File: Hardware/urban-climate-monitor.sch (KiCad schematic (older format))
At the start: 44 parts, among them J1 Conn_ARM_JTAG_SWD_10, U1 AAT1217, U2 TPS27081A, U4 TSD305, U5 TSV911RILT, U6 RFM95W, U7 STM32L412KB

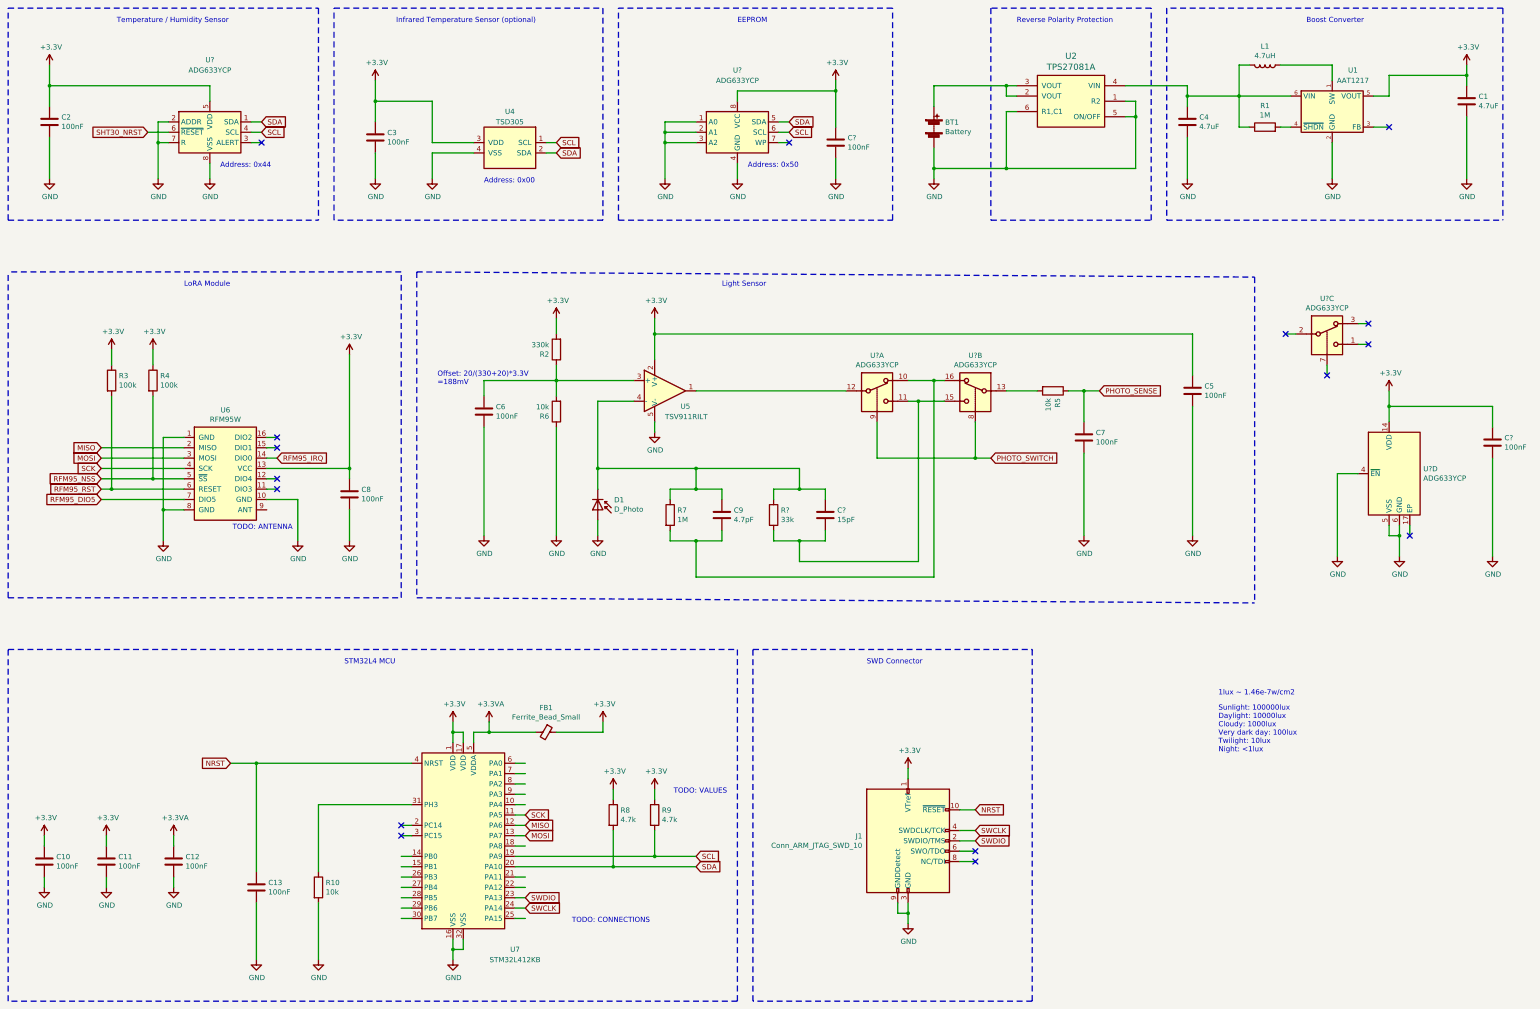
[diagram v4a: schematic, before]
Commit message: Create first revision of PCB, add CubeMX project for PCB sensor node
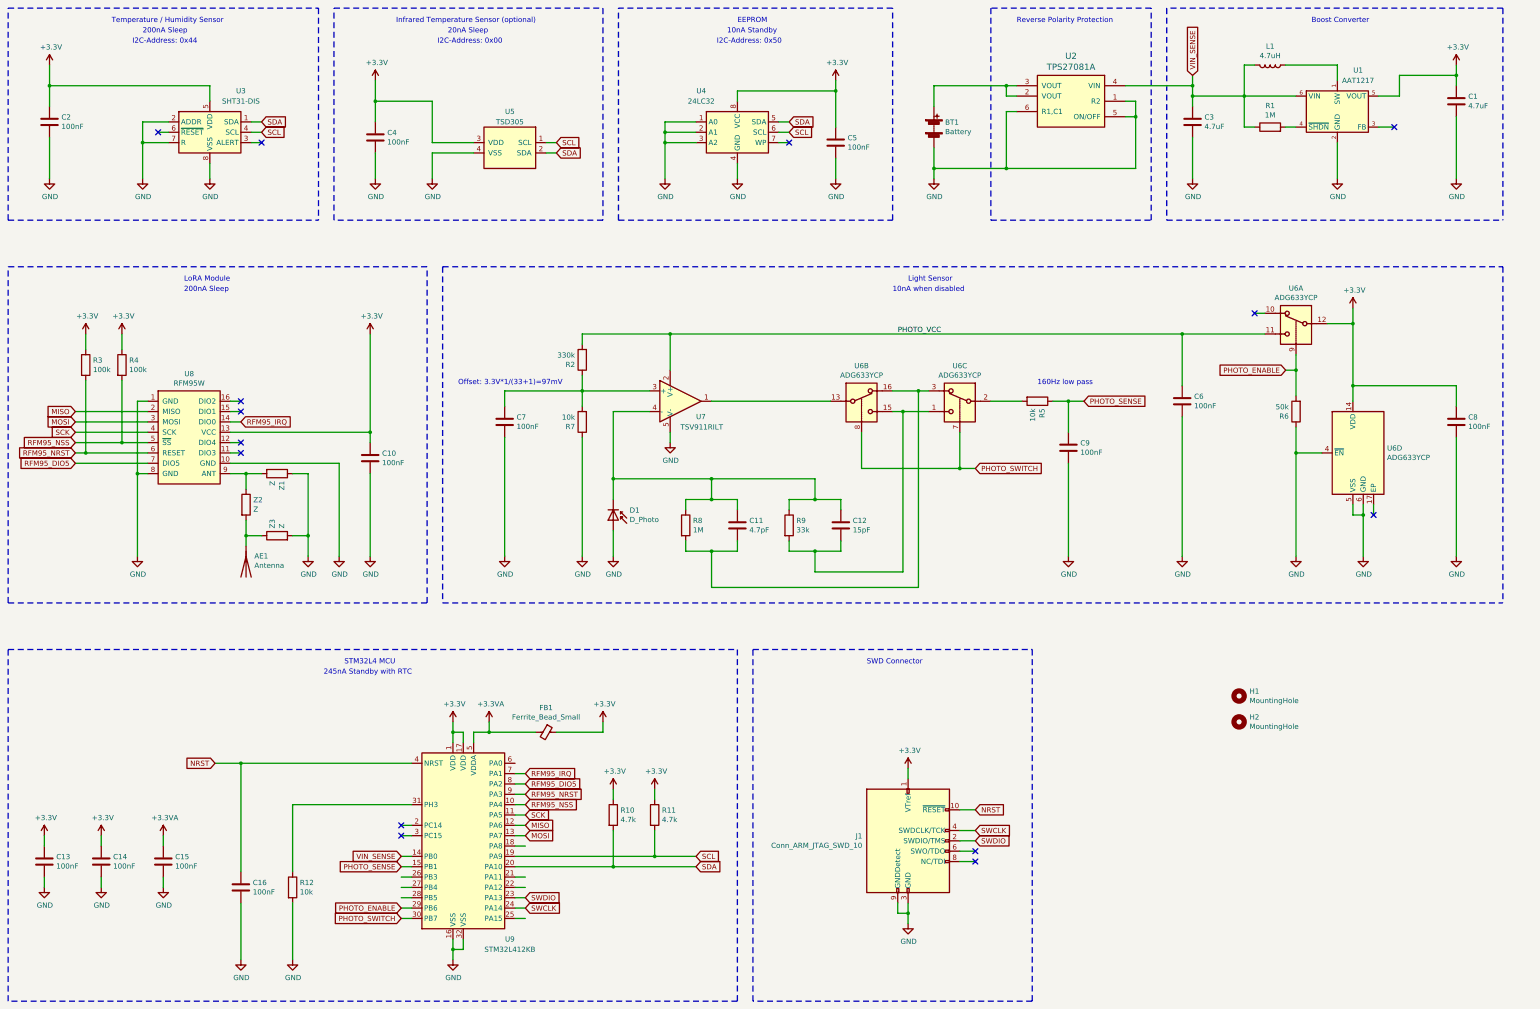
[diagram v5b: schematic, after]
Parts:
- added AE1: Antenna, my-footprints-library:868MHZ_TI_DNO24, symbol Device:Antenna
- added H1, H2: MountingHole, MountingHole:MountingHole_2.2mm_M2, symbol Mechanical:MountingHole
- added R6: 50k, Resistor_SMD:R_0805_2012Metric_Pad1.20x1.40mm_HandSolder, symbol Device:R
- added Z1, Z2, Z3: Z, Resistor_SMD:R_0805_2012Metric_Pad1.20x1.40mm_HandSolder, symbol Device:R
- C1, C2: footprint Capacitor_SMD:C_0805_2012Metric_Pad1.15x1.40mm_HandSolder -> Capacitor_SMD:C_0805_2012Metric_Pad1.18x1.45mm_HandSolder
- C10: renamed from C8; footprint Capacitor_SMD:C_0805_2012Metric_Pad1.15x1.40mm_HandSolder -> Capacitor_SMD:C_0805_2012Metric_Pad1.18x1.45mm_HandSolder
- C11: renamed from C9; footprint Capacitor_SMD:C_0805_2012Metric_Pad1.15x1.40mm_HandSolder -> Capacitor_SMD:C_0805_2012Metric_Pad1.18x1.45mm_HandSolder
- C12, C5, C8: renamed from C?; footprint Capacitor_SMD:C_0805_2012Metric_Pad1.15x1.40mm_HandSolder -> Capacitor_SMD:C_0805_2012Metric_Pad1.18x1.45mm_HandSolder
- C13: renamed from C10; footprint Capacitor_SMD:C_0805_2012Metric_Pad1.15x1.40mm_HandSolder -> Capacitor_SMD:C_0805_2012Metric_Pad1.18x1.45mm_HandSolder
- C14: renamed from C11; footprint Capacitor_SMD:C_0805_2012Metric_Pad1.15x1.40mm_HandSolder -> Capacitor_SMD:C_0805_2012Metric_Pad1.18x1.45mm_HandSolder
- C15: renamed from C12; footprint Capacitor_SMD:C_0805_2012Metric_Pad1.15x1.40mm_HandSolder -> Capacitor_SMD:C_0805_2012Metric_Pad1.18x1.45mm_HandSolder
- C16: renamed from C13; footprint Capacitor_SMD:C_0805_2012Metric_Pad1.15x1.40mm_HandSolder -> Capacitor_SMD:C_0805_2012Metric_Pad1.18x1.45mm_HandSolder
- C3: renamed from C4; footprint Capacitor_SMD:C_0805_2012Metric_Pad1.15x1.40mm_HandSolder -> Capacitor_SMD:C_0805_2012Metric_Pad1.18x1.45mm_HandSolder
- C4: renamed from C3; footprint Capacitor_SMD:C_0805_2012Metric_Pad1.15x1.40mm_HandSolder -> Capacitor_SMD:C_0805_2012Metric_Pad1.18x1.45mm_HandSolder
- C6: renamed from C5; footprint Capacitor_SMD:C_0805_2012Metric_Pad1.15x1.40mm_HandSolder -> Capacitor_SMD:C_0805_2012Metric_Pad1.18x1.45mm_HandSolder
- C7: renamed from C6; footprint Capacitor_SMD:C_0805_2012Metric_Pad1.15x1.40mm_HandSolder -> Capacitor_SMD:C_0805_2012Metric_Pad1.18x1.45mm_HandSolder
- C9: renamed from C7; footprint Capacitor_SMD:C_0805_2012Metric_Pad1.15x1.40mm_HandSolder -> Capacitor_SMD:C_0805_2012Metric_Pad1.18x1.45mm_HandSolder
- D1: footprint (none) -> LED_THT:LED_D5.0mm_Clear
- FB1: footprint (none) -> Inductor_SMD:L_0805_2012Metric_Pad1.05x1.20mm_HandSolder
- R1, R2, R3, R4, R5: footprint Resistor_SMD:R_0805_2012Metric_Pad1.15x1.40mm_HandSolder -> Resistor_SMD:R_0805_2012Metric_Pad1.20x1.40mm_HandSolder
- R10: renamed from R8; footprint Resistor_SMD:R_0805_2012Metric_Pad1.15x1.40mm_HandSolder -> Resistor_SMD:R_0805_2012Metric_Pad1.20x1.40mm_HandSolder
- R11: renamed from R9; footprint Resistor_SMD:R_0805_2012Metric_Pad1.15x1.40mm_HandSolder -> Resistor_SMD:R_0805_2012Metric_Pad1.20x1.40mm_HandSolder
- R12: renamed from R10; footprint Resistor_SMD:R_0805_2012Metric_Pad1.15x1.40mm_HandSolder -> Resistor_SMD:R_0805_2012Metric_Pad1.20x1.40mm_HandSolder
- R7: renamed from R6; footprint Resistor_SMD:R_0805_2012Metric_Pad1.15x1.40mm_HandSolder -> Resistor_SMD:R_0805_2012Metric_Pad1.20x1.40mm_HandSolder
- R8: renamed from R7; footprint Resistor_SMD:R_0805_2012Metric_Pad1.15x1.40mm_HandSolder -> Resistor_SMD:R_0805_2012Metric_Pad1.20x1.40mm_HandSolder
- R9: renamed from R?; footprint Resistor_SMD:R_0805_2012Metric_Pad1.15x1.40mm_HandSolder -> Resistor_SMD:R_0805_2012Metric_Pad1.20x1.40mm_HandSolder
- U3: renamed from U?; value ADG633YCP -> SHT31-DIS; footprint Package_CSP:LFCSP-16-1EP_4x4mm_P0.65mm_EP2.1x2.1mm -> Sensor_Humidity:Sensirion_DFN-8-1EP_2.5x2.5mm_P0.5mm_EP1.1x1.7mm
- U4: renamed from U?; value ADG633YCP -> 24LC32; footprint Package_CSP:LFCSP-16-1EP_4x4mm_P0.65mm_EP2.1x2.1mm -> Package_SO:SOIC-8_3.9x4.9mm_P1.27mm
- U5: renamed from U4; footprint (none) -> my-footprints-library:TSD305
- U6: renamed from U?; footprint Package_CSP:LFCSP-16-1EP_4x4mm_P0.65mm_EP2.1x2.1mm -> Package_SO:TSSOP-16_4.4x5mm_P0.65mm
- U8: renamed from U6; footprint (none) -> my-footprints-library:RFM95W
- renumbered U5 to U7, U7 to U9
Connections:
- net labels added: PHOTO_ENABLE, PHOTO_VCC, RFM95_NRST, VIN_SENSE
- net labels removed: RFM95_RST, SHT30_NRST
- wire segments 244 -> 258
- no-connect marks 16 -> 14
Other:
- note added: "10nA Standby"
- note added: "10nA when disabled"
- note added: "160Hz low pass"
- note added: "200nA Sleep"
- note added: "20nA Sleep"
- note added: "245nA Standby with RTC"
- note added: "I2C-Address: 0x00"
- note added: "I2C-Address: 0x44"
- note added: "I2C-Address: 0x50"
- note added: "Offset: 3.3V*1/(33+1)=97mV"
- note removed: "1lux ~~ 1.46e-7w/cm2"
- note removed: "Address: 0x00"
- note removed: "Address: 0x44"
- note removed: "Address: 0x50"
- note removed: "Offset: 20/(330+20)*3.3V\n=188mV"
- note removed: "Sunlight: 100000lux\nDaylight: 10000lux\nCloudy: 1000lux\nVery dark day: 100lux\nTwilight: 10lux\nNight: <1lux"
- note removed: "TODO: ANTENNA"
- note removed: "TODO: CONNECTIONS\n"
- note removed: "TODO: VALUES"
- moved on the sheet: C1, C10, C11, C12, C14, C15, C16, C3, C6, C7, C8, C9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
